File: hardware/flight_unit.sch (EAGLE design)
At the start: 26 parts, among them IC2 7805T, J1 DCJ0202, J2 CONN_20X2SHROUDED, T1 THERMISTOR-2,5, U1 4MB Flash, U2 4MB Flash, U3 4MB Flash

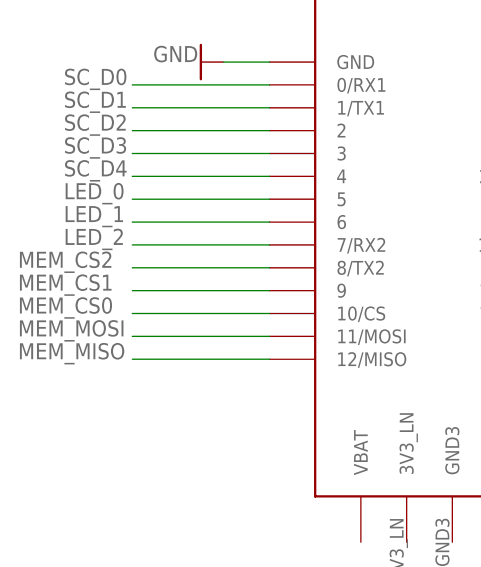
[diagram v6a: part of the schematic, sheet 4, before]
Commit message: added start of fram framework
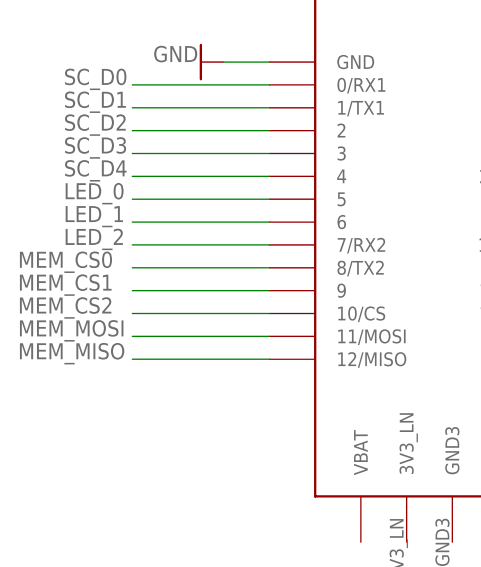
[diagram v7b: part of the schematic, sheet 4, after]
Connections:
- net MEM_CS0: now also U$1.8/TX2; no longer U$1.10/CS
- net MEM_CS2: now also U$1.10/CS; no longer U$1.8/TX2
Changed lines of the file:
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@@
 <net name="MEM_CS0" class="0">
 <segment>
-<pinref part="U$1" gate="G$1" pin="10/CS"/>
-<wire x1="114.3" y1="83.82" x2="99.06" y2="83.82" width="0.1524" layer="91"/>
-<label x="86.36" y="83.82" size="1.778" layer="95"/>
+<pinref part="U$1" gate="G$1" pin="8/TX2"/>
+<wire x1="114.3" y1="88.9" x2="99.06" y2="88.9" width="0.1524" layer="91"/>
+<label x="86.36" y="88.9" size="1.778" layer="95"/>
 </segment>
 </net>
@@
 <wire x1="114.3" y1="86.36" x2="99.06" y2="86.36" width="0.1524" layer="91"/>
 <label x="86.36" y="86.36" size="1.778" layer="95"/>
-</segment>
-</net>
-<net name="MEM_CS2" class="0">
-<segment>
-<pinref part="U$1" gate="G$1" pin="8/TX2"/>
-<wire x1="114.3" y1="88.9" x2="99.06" y2="88.9" width="0.1524" layer="91"/>
-<label x="86.36" y="88.9" size="1.778" layer="95"/>
 </segment>
 </net>
@@
 </segment>
 </net>
+<net name="MEM_CS2" class="0">
+<segment>
+<pinref part="U$1" gate="G$1" pin="10/CS"/>
+<wire x1="114.3" y1="83.82" x2="99.06" y2="83.82" width="0.1524" layer="91"/>
+<label x="86.36" y="83.82" size="1.778" layer="95"/>
+</segment>
+</net>

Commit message: Add files via upload
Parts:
- removed BATTERY: 5V, battery:CR-AA
- removed J1: DCJ0202, con-jack:DCJ0202
- added C1, C2: 0.1uf, capacitor-wima:C2,5-3
- R1: value 1k -> 3.3k
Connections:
- net +3V3: now also C1.1
- net GND: now also C1.2, C2.2; no longer BATTERY.-, J1.2
- net N$1: no longer BATTERY.+
- net N$2: now also C2.1
- net N$4: no longer J1.1
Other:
- note added: "Backup Battery Input"
- note added: "ISS Power Source"
- moved on the sheet: D2
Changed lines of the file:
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@@
 <?xml version="1.0" encoding="utf-8"?>
 <!DOCTYPE eagle SYSTEM "eagle.dtd">
-<eagle version="9.5.1">
+<eagle version="9.6.2">
 <drawing>
 <settings>
@@
 <part name="D1" library="diode" library_urn="urn:adsk.eagle:library:210" deviceset="1N4004" device="" package3d_urn="urn:adsk.eagle:package:43336/1"/>
 <part name="D2" library="diode" library_urn="urn:adsk.eagle:library:210" deviceset="1N4004" device="" package3d_urn="urn:adsk.eagle:package:43336/1"/>
-<part name="R1" library="rcl" library_urn="urn:adsk.eagle:library:334" deviceset="R-US_" device="0207/10" package3d_urn="urn:adsk.eagle:package:23491/1" value="1k">
+<part name="R1" library="rcl" library_urn="urn:adsk.eagle:library:334" deviceset="R-US_" device="0207/10" package3d_urn="urn:adsk.eagle:package:23491/1" value="3.3k">
 <attribute name="SPICEPREFIX" value="1000 Ohm"/>
 </part>
-<part name="BATTERY" library="battery" library_urn="urn:adsk.eagle:library:109" deviceset="CR-AA" device="" package3d_urn="urn:adsk.eagle:package:4582/1" value="5V">
-<attribute name="BATTERY" value="5 V"/>
-</part>
-<part name="J1" library="con-jack" library_urn="urn:adsk.eagle:library:154" deviceset="DCJ0202" device="" package3d_urn="urn:adsk.eagle:package:7491/1"/>
 <part name="IC2" library="linear" library_urn="urn:adsk.eagle:library:262" deviceset="78*" device="T" package3d_urn="urn:adsk.eagle:package:16414/1" technology="05"/>
 <part name="+3V1" library="supply1" deviceset="+3V3" device=""/>
@@
 <part name="J2" library="SparkFun-Connectors" library_urn="urn:adsk.eagle:library:513" deviceset="CONN_20X2" device="SHROUDED" package3d_urn="urn:adsk.eagle:package:38279/1"/>
 <part name="GND" library="SparkFun-PowerSymbols" library_urn="urn:adsk.eagle:library:530" deviceset="GND" device=""/>
-<part name="GND1" library="SparkFun-PowerSymbols" library_urn="urn:adsk.eagle:library:530" deviceset="GND" device=""/>
-<part name="GND2" library="SparkFun-PowerSymbols" library_urn="urn:adsk.eagle:library:530" deviceset="GND" device=""/>
 <part name="GND3" library="SparkFun-PowerSymbols" library_urn="urn:adsk.eagle:library:530" deviceset="GND" device=""/>
 <part name="U$1" library="TEENSY 4.0" deviceset="TEENSY_4.0" device=""/>
@@
 <part name="JP1" library="adafruit" deviceset="PINHD-1X6" device="B"/>
 <part name="U$8" library="microbuilder" deviceset="GND" device=""/>
+<part name="C1" library="capacitor-wima" library_urn="urn:adsk.eagle:library:116" deviceset="C" device="2,5-3" package3d_urn="urn:adsk.eagle:package:5436/1" value="0.1uf"/>
+<part name="GND1" library="SparkFun-PowerSymbols" library_urn="urn:adsk.eagle:library:530" deviceset="GND" device=""/>
+<part name="C2" library="capacitor-wima" library_urn="urn:adsk.eagle:library:116" deviceset="C" device="2,5-3" package3d_urn="urn:adsk.eagle:package:5436/1" value="0.1uf"/>
+<part name="GND2" library="SparkFun-PowerSymbols" library_urn="urn:adsk.eagle:library:530" deviceset="GND" device=""/>
 </parts>
 <sheets>
@@
 </text>
 <text x="82.55" y="161.29" size="5.08" layer="97">Power Regulation and Supply</text>
+<text x="68.58" y="109.22" size="1.778" layer="91">ISS Power Source</text>
+<text x="114.3" y="81.28" size="1.778" layer="91">Backup Battery Input </text>
 </plain>
 <instances>
@@
 <attribute name="VALUE" x="107.95" y="108.1786" size="1.778" layer="96"/>
 </instance>
-<instance part="D2" gate="1" x="132.08" y="100.33" smashed="yes" rot="R90">
-<attribute name="NAME" x="131.5974" y="102.87" size="1.778" layer="95" rot="R90"/>
-<attribute name="VALUE" x="134.3914" y="102.87" size="1.778" layer="96" rot="R90"/>
+<instance part="D2" gate="1" x="129.54" y="100.33" smashed="yes" rot="R90">
+<attribute name="NAME" x="129.0574" y="102.87" size="1.778" layer="95" rot="R90"/>
+<attribute name="VALUE" x="131.8514" y="102.87" size="1.778" layer="96" rot="R90"/>
 </instance>
 <instance part="R1" gate="G$1" x="121.92" y="100.33" smashed="yes" rot="R90">
@@
 <attribute name="SPICEPREFIX" x="121.92" y="100.33" size="1.778" layer="96" rot="R90" display="off"/>
 </instance>
-<instance part="BATTERY" gate="1" x="121.92" y="85.09" smashed="yes" rot="R90">
-<attribute name="NAME" x="118.745" y="80.01" size="1.778" layer="95" rot="R90"/>
-<attribute name="VALUE" x="127" y="82.55" size="1.778" layer="96" rot="R90"/>
-<attribute name="BATTERY" x="121.92" y="85.09" size="1.778" layer="96" rot="R90" display="off"/>
-</instance>
-<instance part="J1" gate="G$1" x="83.82" y="107.95" smashed="yes">
-<attribute name="NAME" x="81.28" y="111.76" size="1.778" layer="95"/>
-<attribute name="VALUE" x="81.28" y="101.6" size="1.778" layer="96"/>
-</instance>
 <instance part="IC2" gate="A1" x="147.32" y="110.49" smashed="yes">
 <attribute name="VALUE" x="139.7" y="113.665" size="1.778" layer="96"/>
@@
 <attribute name="VALUE" x="163.83" y="118.11" size="1.778" layer="96"/>
 </instance>
-<instance part="GND1" gate="1" x="96.52" y="88.9" smashed="yes">
-<attribute name="VALUE" x="96.52" y="88.646" size="1.778" layer="96" align="top-center"/>
-</instance>
-<instance part="GND2" gate="1" x="121.92" y="68.58" smashed="yes">
-<attribute name="VALUE" x="121.92" y="68.326" size="1.778" layer="96" align="top-center"/>
-</instance>
 <instance part="GND3" gate="1" x="147.32" y="93.98" smashed="yes">
 <attribute name="VALUE" x="147.32" y="93.726" size="1.778" layer="96" align="top-center"/>
+</instance>
+<instance part="C1" gate="G$1" x="162.56" y="104.14" smashed="yes">
+<attribute name="NAME" x="164.084" y="104.521" size="1.778" layer="95"/>
+<attribute name="VALUE" x="164.084" y="99.441" size="1.778" layer="96"/>
+</instance>
+<instance part="GND1" gate="1" x="162.56" y="93.98" smashed="yes">
+<attribute name="VALUE" x="162.56" y="93.726" size="1.778" layer="96" align="top-center"/>
+</instance>
+<instance part="C2" gate="G$1" x="134.62" y="104.14" smashed="yes">
+<attribute name="NAME" x="136.144" y="104.521" size="1.778" layer="95"/>
+<attribute name="VALUE" x="136.144" y="99.441" size="1.778" layer="96"/>
+</instance>
+<instance part="GND2" gate="1" x="134.62" y="93.98" smashed="yes">
+<attribute name="VALUE" x="134.62" y="93.726" size="1.778" layer="96" align="top-center"/>
 </instance>
 </instances>
@@
 <net name="N$1" class="0">
 <segment>
-<pinref part="BATTERY" gate="1" pin="+"/>
 <pinref part="R1" gate="G$1" pin="1"/>
-<wire x1="121.92" y1="90.17" x2="121.92" y2="95.25" width="0.1524" layer="91"/>
+<pinref part="D2" gate="1" pin="A"/>
+<wire x1="121.92" y1="95.25" x2="129.54" y2="95.25" width="0.1524" layer="91"/>
+<wire x1="129.54" y1="95.25" x2="129.54" y2="97.79" width="0.1524" layer="91"/>
+<wire x1="121.92" y1="95.25" x2="121.92" y2="83.82" width="0.1524" layer="91"/>
 <junction x="121.92" y="95.25"/>
-<pinref part="D2" gate="1" pin="A"/>
-<wire x1="121.92" y1="95.25" x2="132.08" y2="95.25" width="0.1524" layer="91"/>
-<wire x1="132.08" y1="95.25" x2="132.08" y2="97.79" width="0.1524" layer="91"/>
 </segment>
 </net>
@@
 <junction x="121.92" y="110.49"/>
 <pinref part="D2" gate="1" pin="C"/>
-<wire x1="132.08" y1="110.49" x2="121.92" y2="110.49" width="0.1524" layer="91"/>
-<wire x1="132.08" y1="102.87" x2="132.08" y2="110.49" width="0.1524" layer="91"/>
-<wire x1="132.08" y1="110.49" x2="137.16" y2="110.49" width="0.1524" layer="91"/>
-<junction x="132.08" y="110.49"/>
+<wire x1="129.54" y1="110.49" x2="121.92" y2="110.49" width="0.1524" layer="91"/>
+<wire x1="129.54" y1="102.87" x2="129.54" y2="110.49" width="0.1524" layer="91"/>
+<wire x1="129.54" y1="110.49" x2="137.16" y2="110.49" width="0.1524" layer="91"/>
+<junction x="129.54" y="110.49"/>
 <pinref part="IC2" gate="A1" pin="VI"/>
+<pinref part="C2" gate="G$1" pin="1"/>
+<wire x1="134.62" y1="106.68" x2="134.62" y2="110.49" width="0.1524" layer="91"/>
+<wire x1="134.62" y1="110.49" x2="137.16" y2="110.49" width="0.1524" layer="91"/>
+<junction x="137.16" y="110.49"/>
 </segment>
 </net>
 <net name="N$4" class="0">
 <segment>
-<pinref part="J1" gate="G$1" pin="1"/>
 <pinref part="D1" gate="1" pin="A"/>
 <wire x1="91.44" y1="110.49" x2="102.87" y2="110.49" width="0.1524" layer="91"/>
@@
 <pinref part="IC2" gate="A1" pin="VO"/>
 <pinref part="+3V1" gate="G$1" pin="+3V3"/>
-<wire x1="162.56" y1="115.57" x2="162.56" y2="110.49" width="0.1524" layer="91"/>
+<wire x1="162.56" y1="115.57" x2="162.56" y2="111.76" width="0.1524" layer="91"/>
+<pinref part="C1" gate="G$1" pin="1"/>
+<wire x1="162.56" y1="111.76" x2="162.56" y2="110.49" width="0.1524" layer="91"/>
+<wire x1="162.56" y1="106.68" x2="162.56" y2="110.49" width="0.1524" layer="91"/>
 </segment>
 </net>
 <net name="GND" class="0">
-<segment>
-<pinref part="J1" gate="G$1" pin="2"/>
-<pinref part="GND1" gate="1" pin="GND"/>
-<wire x1="91.44" y1="107.95" x2="96.52" y2="107.95" width="0.1524" layer="91"/>
-<wire x1="96.52" y1="107.95" x2="96.52" y2="91.44" width="0.1524" layer="91"/>
-</segment>
-<segment>
-<pinref part="BATTERY" gate="1" pin="-"/>
-<pinref part="GND2" gate="1" pin="GND"/>
-<wire x1="121.92" y1="80.01" x2="121.92" y2="71.12" width="0.1524" layer="91"/>
-</segment>
 <segment>
 <pinref part="IC2" gate="A1" pin="GND"/>
@@
 <wire x1="147.32" y1="102.87" x2="147.32" y2="96.52" width="0.1524" layer="91"/>
 </segment>
-</net>
+<segment>
+<pinref part="C1" gate="G$1" pin="2"/>
+<pinref part="GND1" gate="1" pin="GND"/>
+<wire x1="162.56" y1="99.06" x2="162.56" y2="96.52" width="0.1524" layer="91"/>
+</segment>
+<segment>
+<pinref part="C2" gate="G$1" pin="2"/>
+<pinref part="GND2" gate="1" pin="GND"/>
+<wire x1="134.62" y1="99.06" x2="134.62" y2="96.52" width="0.1524" layer="91"/>
+</segment>
+</net>
+<net name="N$9" class="0">
+<segment>
+<junction x="134.62" y="110.49"/>
+</segment>
+</net>
